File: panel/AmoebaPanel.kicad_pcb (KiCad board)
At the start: 2 copper layers, 127.8 x 100 mm, 204 parts, among them J1 Conn_01x01_Pin, J10 Conn_01x01_Pin, J11 Conn_01x01_Pin, J12 Conn_01x01_Pin, J13 Conn_01x01_Pin, J14 Conn_01x01_Pin, J15 Conn_01x01_Pin, J16 Conn_01x01_Pin, J17 Conn_01x01_Pin, J18 Conn_01x01_Pin, J19 Conn_01x01_Pin, J2 Conn_01x01_Pin, J20 Conn_01x01_Pin, J21 Conn_01x01_Pin, J22 Conn_01x01_Pin, J23 Conn_01x01_Pin, J24 Conn_01x01_Pin, J25 Conn_01x01_Pin, J26 Conn_01x01_Pin, J27 Conn_01x01_Pin, J28 Conn_01x01_Pin, J29 Conn_01x01_Pin, J3 Conn_01x01_Pin, J30 Conn_01x01_Pin, J31 Conn_01x01_Pin, J32 Conn_01x01_Pin, J33 Conn_01x01_Pin, J34 Conn_01x01_Pin, J35 Conn_01x01_Pin, J36 Conn_01x01_Pin, J37 Conn_01x01_Pin, J38 Conn_01x01_Pin, J39 Conn_01x01_Pin, J4 Conn_01x01_Pin, J40 Conn_01x01_Pin, J41 Conn_01x01_Pin, J42 Conn_01x01_Pin, J43 Conn_01x01_Pin, J44 Conn_01x01_Pin, J45 Conn_01x01_Pin, J46 Conn_01x01_Pin, J47 Conn_01x01_Pin, J48 Conn_01x01_Pin, J49 Conn_01x01_Pin, J5 Conn_01x01_Pin, J50 Conn_01x01_Pin, J51 Conn_01x01_Pin, J52 Conn_01x01_Pin, J53 Conn_01x01_Pin, J54 Conn_01x01_Pin, J55 Conn_01x01_Pin, J56 Conn_01x01_Pin, J57 Conn_01x01_Pin, J58 Conn_01x01_Pin, J59 Conn_01x01_Pin, J6 Conn_01x01_Pin, J60 Conn_01x01_Pin, J61 Conn_01x01_Pin, J62 Conn_01x01_Pin, J63 Conn_01x01_Pin, J64 Conn_01x01_Pin, J65 Conn_01x01_Pin, J66 Conn_01x01_Pin, J67 Conn_01x01_Pin, J68 Conn_01x01_Pin, J69 Conn_01x01_Pin, J7 Conn_01x01_Pin, J70 Conn_01x01_Pin, J71 Conn_01x01_Pin, J72 Conn_01x01_Pin, J73 Conn_01x01_Pin, J74 Conn_01x01_Pin, J75 Conn_01x01_Pin, J76 Conn_01x01_Pin, J77 Conn_01x01_Pin, J78 Conn_01x01_Pin, J79 Conn_01x01_Pin, J8 Conn_01x01_Pin, J80 Conn_01x01_Pin, J81 Conn_01x01_Pin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

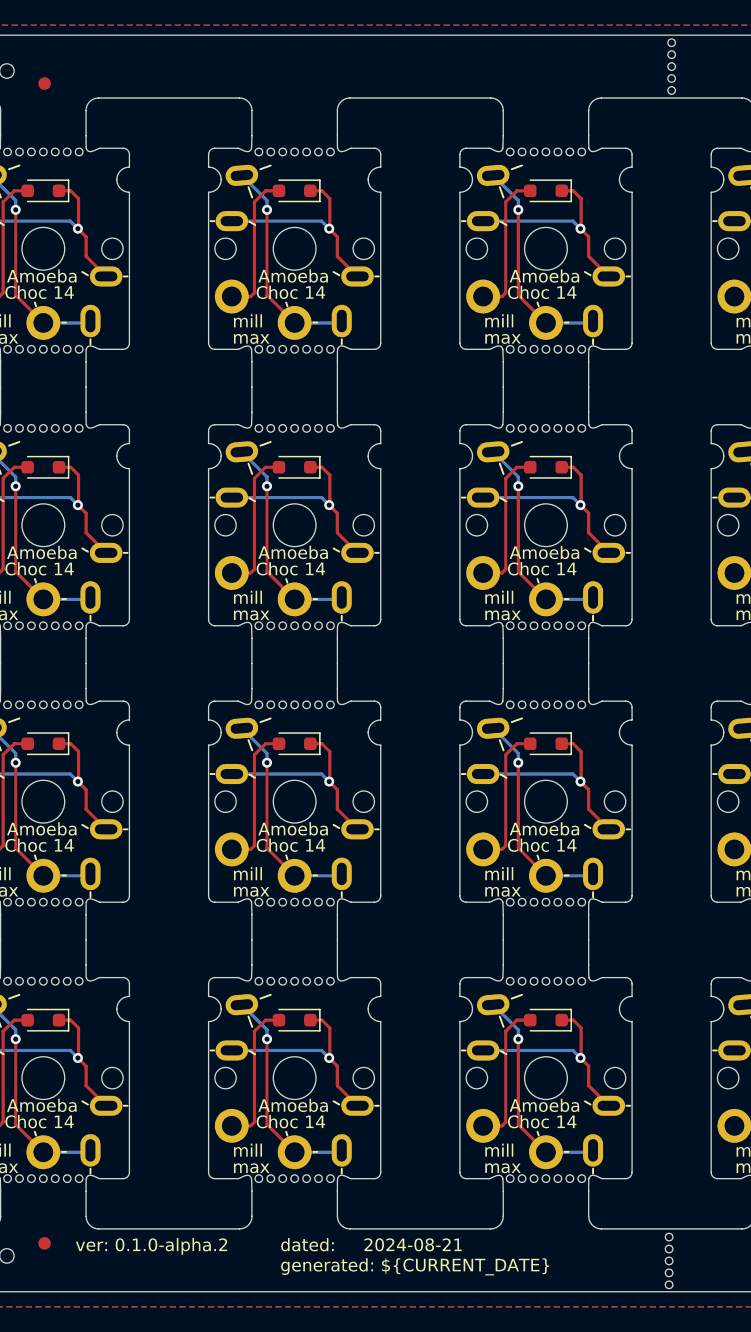
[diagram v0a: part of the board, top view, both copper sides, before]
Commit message: feat(panel): panel shows a sample wiring layoout
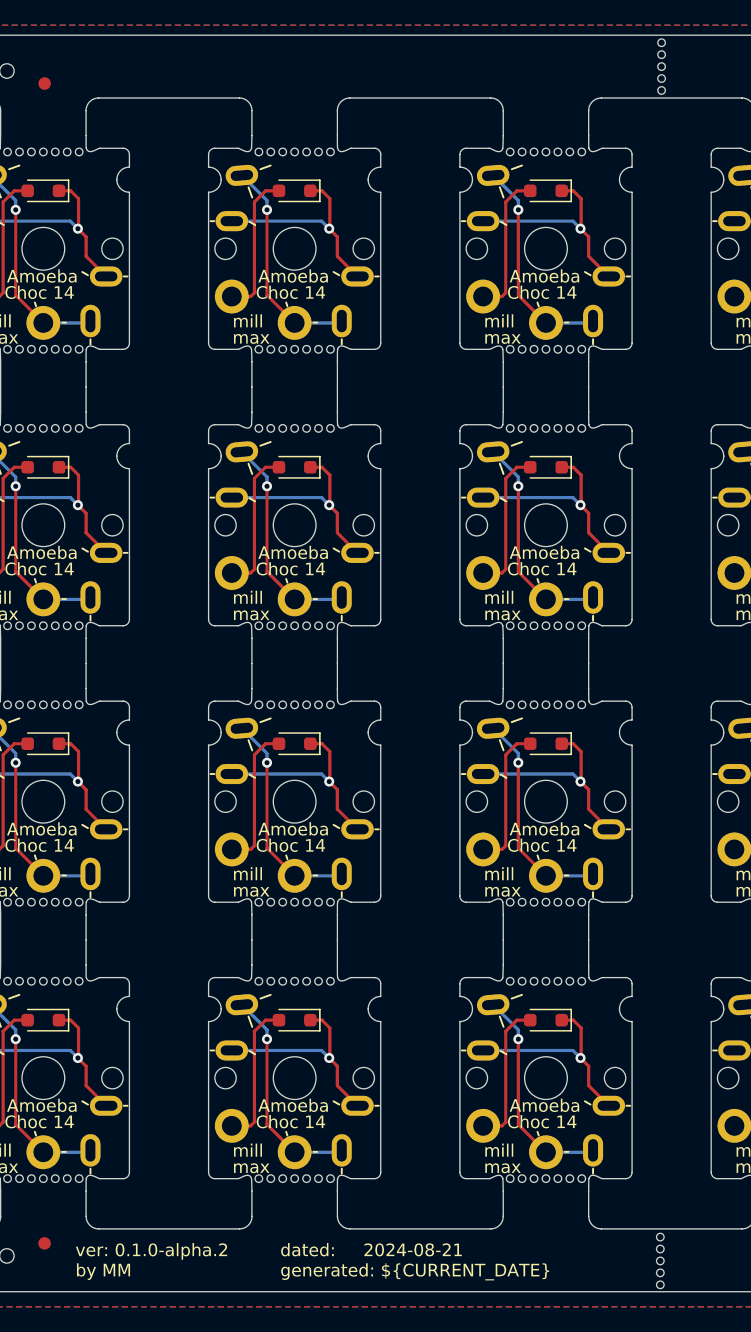
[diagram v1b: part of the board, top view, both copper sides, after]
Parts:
- moved REF** 0.80 mm to (158.3, 53.3)
- moved REF** 0.70 mm to (158.2, 148.3)
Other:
- board text added: "A typical 6 x 4 Dactyl wiring. Adjust for your board."
- board text added: "Long"
- board text added: "Snug"
- board text added: "X"
- board text added: "ver: ${REVISION} by MM"
- board text removed: "ver: ${REVISION}"
